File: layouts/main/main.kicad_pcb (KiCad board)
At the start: 4 copper layers, 20.5 x 20.5 mm, 60 parts

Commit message: wip
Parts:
- moved C8 0.36 mm to (3.47, -6.60), turned to 0 degrees
- moved C7 0.22 mm to (3.47, -7.40)
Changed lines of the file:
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@@
 	(footprint "Murata_Electronics_GRM033R60J104KE19D:C0201"
 		(layer "F.Cu")
-		(at 3.67 -6.3 180)
+		(at 3.47 -6.6)
 		(property "Reference" "C8"
 			(at 0 -0.000166 0)
@@
 		(attr through_hole)
 		(fp_line
+			(start -0.69 0.24)
+			(end -0.69 -0.24)
+			(stroke
+				(width 0.15)
+				(type solid)
+			)
+			(layer "F.SilkS")
+		)
+		(fp_line
+			(start -0.53 -0.39)
+			(end -0.17 -0.39)
+			(stroke
+				(width 0.15)
+				(type solid)
+			)
+			(layer "F.SilkS")
+		)
+		(fp_line
+			(start -0.17 0.39)
+			(end -0.53 0.39)
+			(stroke
+				(width 0.15)
+				(type solid)
+			)
+			(layer "F.SilkS")
+		)
+		(fp_line
+			(start 0.17 0.39)
+			(end 0.53 0.39)
+			(stroke
+				(width 0.15)
+				(type solid)
+			)
+			(layer "F.SilkS")
+		)
+		(fp_line
+			(start 0.53 -0.39)
+			(end 0.17 -0.39)
+			(stroke
+				(width 0.15)
+				(type solid)
+			)
+			(layer "F.SilkS")
+		)
+		(fp_line
 			(start 0.69 0.24)
 			(end 0.69 -0.24)
@@
 			(layer "F.SilkS")
 		)
-		(fp_line
+		(fp_arc
+			(start -0.690333 -0.239643)
+			(mid -0.642835 -0.349658)
+			(end -0.53 -0.39)
+			(stroke
+				(width 0.15)
+				(type solid)
+			)
+			(layer "F.SilkS")
+		)
+		(fp_arc
+			(start -0.529667 0.389644)
+			(mid -0.642347 0.349658)
+			(end -0.69 0.24)
+			(stroke
+				(width 0.15)
+				(type solid)
+			)
+			(layer "F.SilkS")
+		)
+		(fp_arc
 			(start 0.53 -0.39)
-			(end 0.17 -0.39)
-			(stroke
-				(width 0.15)
-				(type solid)
-			)
-			(layer "F.SilkS")
-		)
-		(fp_line
-			(start 0.17 0.39)
-			(end 0.53 0.39)
-			(stroke
-				(width 0.15)
-				(type solid)
-			)
-			(layer "F.SilkS")
-		)
-		(fp_line
-			(start -0.17 0.39)
-			(end -0.53 0.39)
-			(stroke
-				(width 0.15)
-				(type solid)
-			)
-			(layer "F.SilkS")
-		)
-		(fp_line
-			(start -0.53 -0.39)
-			(end -0.17 -0.39)
-			(stroke
-				(width 0.15)
-				(type solid)
-			)
-			(layer "F.SilkS")
-		)
-		(fp_line
-			(start -0.69 0.24)
-			(end -0.69 -0.24)
+			(mid 0.642835 -0.349658)
+			(end 0.690333 -0.239643)
 			(stroke
 				(width 0.15)
@@
 			(layer "F.SilkS")
 		)
-		(fp_arc
-			(start 0.53 -0.39)
-			(mid 0.642835 -0.349658)
-			(end 0.690333 -0.239643)
-			(stroke
-				(width 0.15)
-				(type solid)
-			)
-			(layer "F.SilkS")
-		)
-		(fp_arc
-			(start -0.529667 0.389644)
-			(mid -0.642347 0.349658)
-			(end -0.69 0.24)
-			(stroke
-				(width 0.15)
-				(type solid)
-			)
-			(layer "F.SilkS")
-		)
-		(fp_arc
-			(start -0.690333 -0.239643)
-			(mid -0.642835 -0.349658)
-			(end -0.53 -0.39)
-			(stroke
-				(width 0.15)
-				(type solid)
-			)
-			(layer "F.SilkS")
-		)
 		(fp_circle
 			(center -0.3 0.15)
@@
 		)
 		(pad "1" smd rect
-			(at -0.27 0 180)
+			(at -0.27 0)
 			(size 0.37 0.32)
 			(layers "F.Cu" "F.Mask" "F.Paste")
@@
 		)
 		(pad "2" smd rect
-			(at 0.27 0 180)
+			(at 0.27 0)
 			(size 0.37 0.32)
 			(layers "F.Cu" "F.Mask" "F.Paste")
@@
 	(footprint "Murata_Electronics_GRM033R60J104KE19D:C0201"
 		(layer "F.Cu")
-		(at 3.67 -7.3)
+		(at 3.47 -7.4)
 		(property "Reference" "C7"
 			(at 0 -0.000167 0)

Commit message: wip
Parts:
- moved R4 6.52 mm to (-5.80, -4.56), turned to 90 degrees
- moved R2 2.79 mm to (-2.50, -5.86), turned to -90 degrees
- moved REF** 2.39 mm to (-3.80, -6.30)
- moved REF** 1.43 mm to (-6.40, -6.30)
- moved REF** 1.20 mm to (-7.30, -5.30)
- moved R3 0.30 mm to (-2.50, -6.96)
- moved REF** 0.22 mm to (-5.10, -6.30)
- moved R8 0.20 mm to (-3.40, -4.56)
- moved R9 0.20 mm to (-4.60, -4.56)
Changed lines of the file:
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@@
 	(footprint "POGO_PAD:POGO_PAD"
 		(layer "F.Cu")
-		(at -7 -5)
+		(at -6.4 -6.3)
 		(property "Reference" "REF**"
 			(at 0 0 0)
@@
 	(footprint "UNI_ROYAL_0201WMF1002TEE:R0201"
 		(layer "F.Cu")
-		(at -3.2 -4.56 90)
+		(at -3.4 -4.56 90)
 		(property "Reference" "R8"
 			(at 0 0 0)
@@
 	(footprint "POGO_PAD:POGO_PAD"
 		(layer "F.Cu")
-		(at -5.2 -6.1)
+		(at -5.1 -6.3)
 		(property "Reference" "REF**"
 			(at 0 0 0)
@@
 	(footprint "UNI_ROYAL_0201WMF4701TEE:R0201"
 		(layer "F.Cu")
-		(at -2.5 -6.66 -90)
+		(at -2.5 -6.96 -90)
 		(property "Reference" "R3"
 			(at 0 0 0)
@@
 	(footprint "UNI_ROYAL_0201WMJ0330TEE:R0201"
 		(layer "F.Cu")
-		(at 0.66 -3.7)
+		(at -5.8 -4.56 90)
 		(property "Reference" "R4"
-			(at 0 0 90)
+			(at 0 0 0)
 			(layer "F.SilkS")
 			(effects
@@
 		)
 		(property "Value" "33Ω ±5% 50mW"
-			(at 0 0 90)
+			(at 0 0 0)
 			(layer "F.Fab")
 			(effects
@@
 		)
 		(property "Datasheet" "https://wmsc.lcsc.com/wmsc/upload/file/pdf/v2/lcsc/2205312145_UNI-ROYAL-Uniroyal-Elec-0201WMJ0330TEE_C423356.pdf"
-			(at 0 0 0)
+			(at 0 0 90)
 			(layer "User.9")
 			(hide yes)
@@
 		)
 		(property "Description" ""
-			(at 0 0 0)
+			(at 0 0 90)
 			(layer "F.Fab")
 			(hide yes)
@@
 		)
 		(property "checksum" "ab7e766c14a60369aa28116b01504e6514a3eb1616d1f71d480e335b1894b8ea"
-			(at 0 0 90)
+			(at 0 0 0)
 			(layer "User.9")
 			(hide yes)
@@
 		)
 		(property "__atopile_lib_fp_hash__" "5c987cfc-286b-6ffe-d212-f95475017c44"
-			(at 0 0 90)
+			(at 0 0 0)
 			(layer "User.9")
 			(hide yes)
@@
 		)
 		(property "LCSC" "C423356"
-			(at 0 0 0)
+			(at 0 0 90)
 			(layer "User.9")
 			(hide yes)
@@
 		)
 		(property "Manufacturer" "UNI-ROYAL(Uniroyal Elec)"
-			(at 0 0 0)
+			(at 0 0 90)
 			(layer "User.9")
 			(hide yes)
@@
 		)
 		(property "Partnumber" "0201WMJ0330TEE"
-			(at 0 0 0)
+			(at 0 0 90)
 			(layer "User.9")
 			(hide yes)
@@
 		)
 		(property "PARAM_max_power" "{\"type\": \"Quantity_Set_Discrete\", \"data\": {\"intervals\": {\"type\": \"Numeric_Interval_Disjoint\", \"data\": {\"intervals\": [{\"type\": \"Numeric_Interval\", \"data\": {\"min\": 0.05, \"max\": 0.05}}]}}, \"unit\": \"watt\"}}"
-			(at 0 0 0)
+			(at 0 0 90)
 			(layer "User.9")
 			(hide yes)
@@
 		)
 		(property "PARAM_max_voltage" "{\"type\": \"Quantity_Set_Discrete\", \"data\": {\"intervals\": {\"type\": \"Numeric_Interval_Disjoint\", \"data\": {\"intervals\": [{\"type\": \"Numeric_Interval\", \"data\": {\"min\": 25.0, \"max\": 25.0}}]}}, \"unit\": \"volt\"}}"
-			(at 0 0 0)
+			(at 0 0 90)
 			(layer "User.9")
 			(hide yes)
@@
 		)
 		(property "PARAM_resistance" "{\"type\": \"Quantity_Interval_Disjoint\", \"data\": {\"intervals\": {\"type\": \"Numeric_Interval_Disjoint\", \"data\": {\"intervals\": [{\"type\": \"Numeric_Interval\", \"data\": {\"min\": 31.349999975413084, \"max\": 34.650000024586916}}]}}, \"unit\": \"ohm\"}}"
-			(at 0 0 0)
+			(at 0 0 90)
 			(layer "User.9")
 			(hide yes)
@@
 		)
 		(property "atopile_address" "r_nand_clk"
-			(at 0 0 0)
+			(at 0 0 90)
 			(layer "User.9")
 			(hide yes)
@@
 		(attr through_hole)
 		(fp_line
-			(start -0.62 -0.39)
-			(end -0.17 -0.39)
+			(start 0.62 -0.39)
+			(end 0.17 -0.39)
 			(stroke
 				(width 0.15)
@@
 		)
 		(fp_line
-			(start -0.62 0.39)
-			(end -0.62 -0.39)
+			(start -0.62 -0.39)
+			(end -0.17 -0.39)
 			(stroke
 				(width 0.15)
@@
 		)
 		(fp_line
-			(start -0.17 0.39)
-			(end -0.62 0.39)
+			(start 0.62 0.39)
+			(end 0.62 -0.39)
 			(stroke
 				(width 0.15)
@@
 		)
 		(fp_line
-			(start 0.62 -0.39)
-			(end 0.17 -0.39)
+			(start -0.17 0.39)
+			(end -0.62 0.39)
 			(stroke
 				(width 0.15)
@@
 		)
 		(fp_line
-			(start 0.62 0.39)
-			(end 0.62 -0.39)
+			(start -0.62 0.39)
+			(end -0.62 -0.39)
 			(stroke
 				(width 0.15)
@@
 		)
 		(fp_text user "${REFERENCE}"
-			(at 0 0 90)
+			(at 0 0 0)
 			(layer "F.SilkS")
 			(effects
@@
 		)
 		(fp_text user "${REFERENCE}"
-			(at 0 0 90)
+			(at 0 0 0)
 			(layer "F.Fab")
 			(effects
@@
 		)
 		(pad "1" smd rect
-			(at -0.24 0)
+			(at -0.24 0 90)
 			(size 0.3 0.32)
 			(layers "F.Cu" "F.Mask" "F.Paste")
@@
 		)
 		(pad "2" smd rect
-			(at 0.24 0)
+			(at 0.24 0 90)
 			(size 0.3 0.32)
 			(layers "F.Cu" "F.Mask" "F.Paste")
@@
 	(footprint "POGO_PAD:POGO_PAD"
 		(layer "F.Cu")
-		(at -6.4 -6.1)
+		(at -7.3 -5.3)
 		(property "Reference" "REF**"
 			(at 0 0 0)
@@
 	(footprint "POGO_PAD:POGO_PAD"
 		(layer "F.Cu")
-		(at -5.8 -5)
+		(at -3.8 -6.3)
 		(property "Reference" "REF**"
 			(at 0 0 0)
@@
 	(footprint "UNI_ROYAL_0201WMF4701TEE:R0201"
 		(layer "F.Cu")
-		(at -0.74 -3.7)
+		(at -2.5 -5.86 -90)
 		(property "Reference" "R2"
-			(at 0 0 0)
+			(at 0 0 90)
 			(layer "F.SilkS")
 			(effects
@@
 		)
 		(property "Value" "4.7kΩ ±1% 50mW"
-			(at 0 0 0)
+			(at 0 0 90)
 			(layer "F.Fab")
 			(effects
@@
 		)
 		(property "Datasheet" "https://wmsc.lcsc.com/wmsc/upload/file/pdf/v2/lcsc/2205311945_UNI-ROYAL-Uniroyal-Elec-0201WMF4701TEE_C270346.pdf"
-			(at 0 0 0)
+			(at 0 0 90)
 			(layer "User.9")
 			(hide yes)
@@
 		)
 		(property "Description" ""
-			(at 0 0 0)
+			(at 0 0 90)
 			(layer "F.Fab")
 			(hide yes)
@@
 		)
 		(property "checksum" "8334129e8d68cc94feb6f24d4494287d4e5c79980c878904c53191d3ecd9f05e"
-			(at 0 0 0)
+			(at 0 0 90)
 			(layer "User.9")
 			(hide yes)
@@
 		)
 		(property "__atopile_lib_fp_hash__" "2b7c5f96-36d0-b881-fd7f-66c187796e91"
-			(at 0 0 0)
+			(at 0 0 90)
 			(layer "User.9")
 			(hide yes)
@@
 		)
 		(property "LCSC" "C270346"
-			(at 0 0 0)
+			(at 0 0 90)
 			(layer "User.9")
 			(hide yes)
@@
 		)
 		(property "Manufacturer" "UNI-ROYAL(Uniroyal Elec)"
-			(at 0 0 0)
+			(at 0 0 90)
 			(layer "User.9")
 			(hide yes)
@@
 		)
 		(property "Partnumber" "0201WMF4701TEE"
-			(at 0 0 0)
+			(at 0 0 90)
 			(layer "User.9")
 			(hide yes)
@@
 		)
 		(property "PARAM_max_power" "{\"type\": \"Quantity_Set_Discrete\", \"data\": {\"intervals\": {\"type\": \"Numeric_Interval_Disjoint\", \"data\": {\"intervals\": [{\"type\": \"Numeric_Interval\", \"data\": {\"min\": 0.05, \"max\": 0.05}}]}}, \"unit\": \"watt\"}}"
-			(at 0 0 0)
+			(at 0 0 90)
 			(layer "User.9")
 			(hide yes)
@@
 		)
 		(property "PARAM_max_voltage" "{\"type\": \"Quantity_Set_Discrete\", \"data\": {\"intervals\": {\"type\": \"Numeric_Interval_Disjoint\", \"data\": {\"intervals\": [{\"type\": \"Numeric_Interval\", \"data\": {\"min\": 25.0, \"max\": 25.0}}]}}, \"unit\": \"volt\"}}"
-			(at 0 0 0)
+			(at 0 0 90)
 			(layer "User.9")
 			(hide yes)
@@
 		)
 		(property "PARAM_resistance" "{\"type\": \"Quantity_Interval_Disjoint\", \"data\": {\"intervals\": {\"type\": \"Numeric_Interval_Disjoint\", \"data\": {\"intervals\": [{\"type\": \"Numeric_Interval\", \"data\": {\"min\": 4653.000001050532, \"max\": 4746.999998949468}}]}}, \"unit\": \"ohm\"}}"
-			(at 0 0 0)
+			(at 0 0 90)
 			(layer "User.9")
 			(hide yes)
@@
 		)
 		(property "atopile_address" "r_i2c_scl"
-			(at 0 0 0)
+			(at 0 0 90)
 			(layer "User.9")
 			(hide yes)
@@
 		(attr through_hole)
 		(fp_line
-			(start -0.62 -0.39)
-			(end -0.17 -0.39)
+			(start -0.62 0.39)
+			(end -0.62 -0.39)
 			(stroke
 				(width 0.15)
@@
 		)
 		(fp_line
-			(start -0.62 0.39)
-			(end -0.62 -0.39)
+			(start -0.17 0.39)
+			(end -0.62 0.39)
 			(stroke
 				(width 0.15)
@@
 		)
 		(fp_line
-			(start -0.17 0.39)
-			(end -0.62 0.39)
+			(start 0.17 0.39)
+			(end 0.62 0.39)
 			(stroke
 				(width 0.15)
@@
 		)
 		(fp_line
-			(start 0.17 0.39)
-			(end 0.62 0.39)
+			(start 0.62 0.39)
+			(end 0.62 -0.39)
 			(stroke
 				(width 0.15)
@@
 		)
 		(fp_line
-			(start 0.62 -0.39)
-			(end 0.17 -0.39)
+			(start -0.62 -0.39)
+			(end -0.17 -0.39)
 			(stroke
 				(width 0.15)
@@
 		)
 		(fp_line
-			(start 0.62 0.39)
-			(end 0.62 -0.39)
+			(start 0.62 -0.39)
+			(end 0.17 -0.39)
 			(stroke
 				(width 0.15)
@@
 		)
 		(fp_text user "${REFERENCE}"
-			(at 0 0 0)
+			(at 0 0 90)
 			(layer "F.SilkS")
 			(effects
@@
 		)
 		(fp_text user "${REFERENCE}"
-			(at 0 0 0)
+			(at 0 0 90)
 			(layer "F.Fab")
 			(effects
@@
 		)
 		(pad "1" smd rect
-			(at -0.24 0)
+			(at -0.24 0 270)
 			(size 0.3 0.32)
 			(layers "F.Cu" "F.Mask" "F.Paste")
@@
 		)
 		(pad "2" smd rect
-			(at 0.24 0)
+			(at 0.24 0 270)
 			(size 0.3 0.32)
 			(layers "F.Cu" "F.Mask" "F.Paste")
@@
 	(footprint "UNI_ROYAL_0201WMF1002TEE:R0201"
 		(layer "F.Cu")
-		(at -4.4 -4.56 90)
+		(at -4.6 -4.56 90)
 		(property "Reference" "R9"
 			(at 0 0 0)

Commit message: wip
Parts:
- moved C13 1.25 mm to (4.80, -3.33)
- moved R14 0.84 mm to (2.40, -3.26)
- moved C21 0.54 mm to (4.10, -3.52), turned to 90 degrees
- moved R10 0.20 mm to (-0.76, -2.50)
- moved R13 0.09 mm to (0.66, -2.50)
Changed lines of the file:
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@@
 	(footprint "UNI_ROYAL_0201WMF0000TEE:R0201"
 		(layer "F.Cu")
-		(at -0.5625 -2.55 180)
+		(at -0.76 -2.5 180)
 		(property "Reference" "R10"
 			(at 0 0 0)
@@
 	(footprint "YAGEO_RC0201FR_07150KL:R0201"
 		(layer "F.Cu")
-		(at 3.2375 -3.21 90)
+		(at 2.4 -3.26 90)
 		(property "Reference" "R14"
 			(at 0 0 0)
@@
 	(footprint "Murata_Electronics_GRM033R60J104KE19D:C0201"
 		(layer "F.Cu")
-		(at 6.0375 -3.48 90)
+		(at 4.8 -3.33 90)
 		(property "Reference" "C13"
 			(at 0 -0.000166 90)
@@
 	(footprint "Samsung_Electro_Mechanics_CL05A105KA5NQNC:C0402"
 		(layer "F.Cu")
-		(at 4.6175 -3.35 180)
+		(at 4.1 -3.52 90)
 		(property "Reference" "C21"
-			(at 0 0 0)
+			(at 0 0 90)
 			(layer "F.SilkS")
 			(effects
@@
 		)
 		(property "Value" "1µF ±10% 25V X5R"
-			(at 0 0 0)
+			(at 0 0 90)
 			(layer "F.Fab")
 			(effects
@@
 		)
 		(property "Datasheet" "https://www.lcsc.com/datasheet/lcsc_datasheet_2304140030_Samsung-Electro-Mechanics-CL05A105KA5NQNC_C52923.pdf"
-			(at 0 0 0)
+			(at 0 0 90)
 			(layer "User.9")
 			(hide yes)
@@
 		)
 		(property "Description" ""
-			(at 0 0 0)
+			(at 0 0 90)
 			(layer "F.Fab")
 			(hide yes)
@@
 		)
 		(property "checksum" "c4552cab8ba94b7b2294d619195d3584771a66b6df67e026bc6e8196d517b938"
-			(at 0 0 0)
+			(at 0 0 90)
 			(layer "User.9")
 			(hide yes)
@@
 		)
 		(property "__atopile_lib_fp_hash__" "e1042a3b-4b38-6816-2d7d-270ba4226139"
-			(at 0 0 0)
+			(at 0 0 90)
 			(layer "User.9")
 			(hide yes)
@@
 		)
 		(property "LCSC" "C52923"
-			(at 0 0 0)
+			(at 0 0 90)
 			(layer "User.9")
 			(hide yes)
@@
 		)
 		(property "Manufacturer" "Samsung Electro-Mechanics"
-			(at 0 0 0)
+			(at 0 0 90)
 			(layer "User.9")
 			(hide yes)
@@
 		)
 		(property "Partnumber" "CL05A105KA5NQNC"
-			(at 0 0 0)
+			(at 0 0 90)
 			(layer "User.9")
 			(hide yes)
@@
 		)
 		(property "PARAM_capacitance" "{\"type\": \"Quantity_Interval_Disjoint\", \"data\": {\"intervals\": {\"type\": \"Numeric_Interval_Disjoint\", \"data\": {\"intervals\": [{\"type\": \"Numeric_Interval\", \"data\": {\"min\": 8.99999999e-07, \"max\": 1.100000001e-06}}]}}, \"unit\": \"farad\"}}"
-			(at 0 0 0)
+			(at 0 0 90)
 			(layer "User.9")
 			(hide yes)
@@
 		)
 		(property "PARAM_max_voltage" "{\"type\": \"Quantity_Set_Discrete\", \"data\": {\"intervals\": {\"type\": \"Numeric_Interval_Disjoint\", \"data\": {\"intervals\": [{\"type\": \"Numeric_Interval\", \"data\": {\"min\": 25.0, \"max\": 25.0}}]}}, \"unit\": \"volt\"}}"
-			(at 0 0 0)
+			(at 0 0 90)
 			(layer "User.9")
 			(hide yes)
@@
 		)
 		(property "PARAM_temperature_coefficient" "{\"type\": \"EnumSet\", \"data\": {\"elements\": [{\"name\": \"X5R\"}], \"enum\": {\"name\": \"TemperatureCoefficient\", \"values\": {\"Y5V\": 1, \"Z5U\": 2, \"X7S\": 3, \"X5R\": 4, \"X6R\": 5, \"X7R\": 6, \"X8R\": 7, \"C0G\": 8}}}}"
-			(at 0 0 0)
+			(at 0 0 90)
 			(layer "User.9")
 			(hide yes)
@@
 		)
 		(property "atopile_address" "c_vddio_bulk"
-			(at 0 0 0)
+			(at 0 0 90)
 			(layer "User.9")
 			(hide yes)
@@
 		(attr smd)
 		(fp_line
-			(start 0.87 -0.35)
-			(end 0.87 0.35)
+			(start 0.22 -0.5)
+			(end 0.72 -0.5)
 			(stroke
 				(width 0.15)
@@
 		)
 		(fp_line
-			(start 0.72 0.5)
-			(end 0.22 0.5)
+			(start -0.72 -0.5)
+			(end -0.22 -0.5)
 			(stroke
 				(width 0.15)
@@
 		)
 		(fp_line
-			(start 0.22 -0.5)
-			(end 0.72 -0.5)
+			(start 0.87 -0.35)
+			(end 0.87 0.35)
 			(stroke
 				(width 0.15)
@@
 		)
 		(fp_line
-			(start -0.22 0.5)
-			(end -0.72 0.5)
+			(start -0.87 0.35)
+			(end -0.87 -0.35)
 			(stroke
 				(width 0.15)
@@
 		)
 		(fp_line
-			(start -0.72 -0.5)
-			(end -0.22 -0.5)
+			(start 0.72 0.5)
+			(end 0.22 0.5)
 			(stroke
 				(width 0.15)
@@
 		)
 		(fp_line
-			(start -0.87 0.35)
-			(end -0.87 -0.35)
+			(start -0.22 0.5)
+			(end -0.72 0.5)
 			(stroke
 				(width 0.15)
@@
 		)
 		(fp_arc
-			(start 0.87 0.35)
-			(mid 0.826066 0.456066)
-			(end 0.72 0.5)
+			(start 0.72 -0.5)
+			(mid 0.826066 -0.456066)
+			(end 0.87 -0.35)
 			(stroke
 				(width 0.15)
@@
 		)
 		(fp_arc
-			(start 0.72 -0.5)
-			(mid 0.826066 -0.456066)
-			(end 0.87 -0.35)
+			(start -0.87 -0.35)
+			(mid -0.826066 -0.456066)
+			(end -0.72 -0.5)
 			(stroke
 				(width 0.15)
@@
 		)
 		(fp_arc
-			(start -0.72 0.5)
-			(mid -0.826066 0.456066)
-			(end -0.87 0.35)
+			(start 0.87 0.35)
+			(mid 0.826066 0.456066)
+			(end 0.72 0.5)
 			(stroke
 				(width 0.15)
@@
 		)
 		(fp_arc
-			(start -0.87 -0.35)
-			(mid -0.826066 -0.456066)
-			(end -0.72 -0.5)
+			(start -0.72 0.5)
+			(mid -0.826066 0.456066)
+			(end -0.87 0.35)
 			(stroke
 				(width 0.15)
@@
 		)
 		(fp_text user "${REFERENCE}"
-			(at 0 0 0)
+			(at 0 0 90)
 			(layer "F.SilkS")
 			(effects
@@
 		)
 		(fp_text user "${REFERENCE}"
-			(at 0 0 0)
+			(at 0 0 90)
 			(layer "F.Fab")
 			(effects
@@
 		)
 		(pad "1" smd rect
-			(at -0.42 0 180)
+			(at -0.42 0 90)
 			(size 0.5 0.54)
 			(layers "F.Cu" "F.Mask" "F.Paste")
@@
 		)
 		(pad "2" smd rect
-			(at 0.42 0 180)
+			(at 0.42 0 90)
 			(size 0.5 0.54)
 			(layers "F.Cu" "F.Mask" "F.Paste")
@@
 		(at 6.7 -5.5)
 		(property "Reference" "REF**"
-			(at 1.3 0 0)
+			(at 0 0 0)
 			(layer "F.SilkS")
 			(effects
@@
 	(footprint "UNI_ROYAL_0201WMF4702TEE:R0201"
 		(layer "F.Cu")
-		(at 0.7375 -2.55 180)
+		(at 0.66 -2.5 180)
 		(property "Reference" "R13"
 			(at 0 0 90)

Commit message: wip
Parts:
- moved C11 0.28 mm to (-2.38, 5.00)
- moved C10 0.10 mm to (-3.60, 5.17)
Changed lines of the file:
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@@
 	(footprint "Murata_Electronics_GRM033R60J104KE19D:C0201"
 		(layer "F.Cu")
-		(at -3.6 5.27 -90)
+		(at -3.6 5.17 -90)
 		(property "Reference" "C10"
 			(at 0 -0.000167 0)
@@
 	(footprint "Samsung_Electro_Mechanics_CL05A225MQ5NSNC:C0402"
 		(layer "F.Cu")
-		(at -2.18 5.2)
+		(at -2.38 5)
 		(property "Reference" "C11"
 			(at 0 0 90)

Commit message: wip
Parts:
- moved R15 0.36 mm to (-1.20, 6.52)
- moved R11 0.20 mm to (-3.56, 8.80)
- moved C6 0.11 mm to (-5.63, 6.80)
- moved C5 0.10 mm to (-1.50, 7.97)
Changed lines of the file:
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@@
 	(footprint "Murata_Electronics_GRM033R60J104KE19D:C0201"
 		(layer "F.Cu")
-		(at -5.67 6.7 180)
+		(at -5.63 6.8 180)
 		(property "Reference" "C6"
 			(at 0 -0.000166 0)
@@
 	(footprint "UNI_ROYAL_0201WMJ0330TEE:R0201"
 		(layer "F.Cu")
-		(at -3.76 8.8)
+		(at -3.56 8.8)
 		(property "Reference" "R11"
 			(at 0 0 90)
@@
 	(footprint "DNP_RES_0201:DNP_RES_0201"
 		(layer "F.Cu")
-		(at -1.4 6.82 -90)
+		(at -1.2 6.52 -90)
 		(property "Reference" "R15"
 			(at 0 0 90)
@@
 	(footprint "Murata_Electronics_GRM033R60J104KE19D:C0201"
 		(layer "F.Cu")
-		(at -1.4 7.97 -90)
+		(at -1.5 7.97 -90)
 		(property "Reference" "C5"
 			(at 0 -0.000167 90)

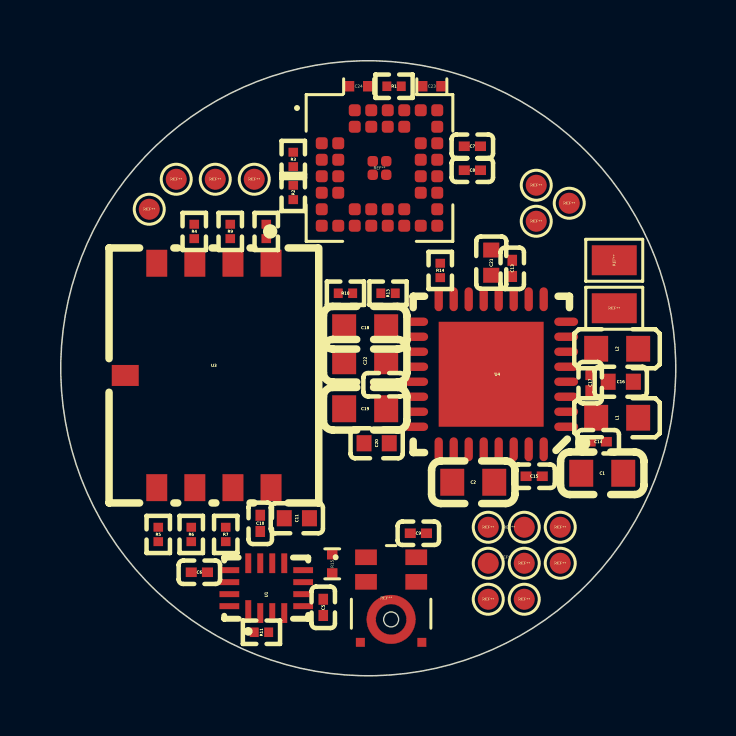
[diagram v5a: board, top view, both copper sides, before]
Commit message: assign reference designators to mcu and mic
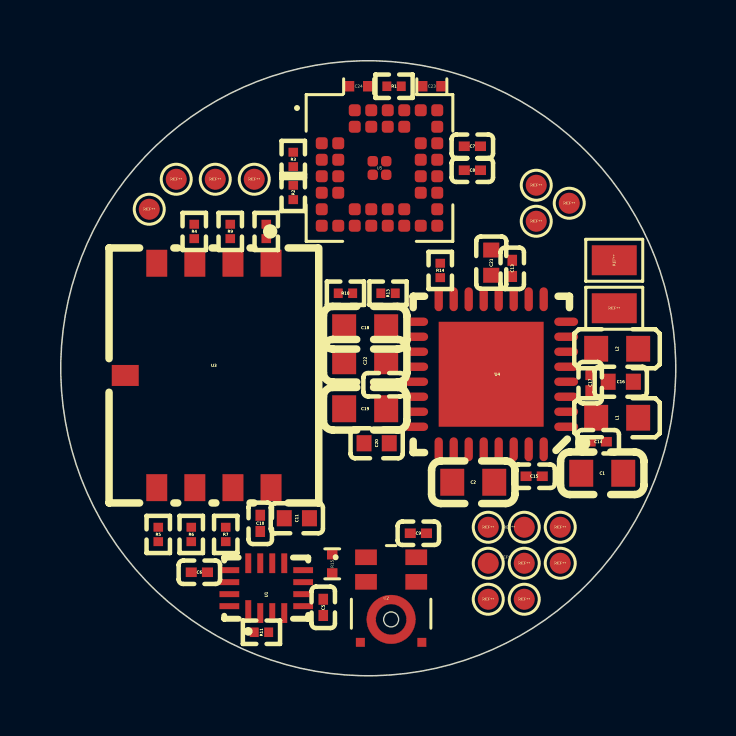
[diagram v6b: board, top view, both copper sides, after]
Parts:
- renumbered REF** to U2, REF** to U5
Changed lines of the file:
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@@
 		(layer "F.Cu")
 		(at 0.7625 7.662)
-		(property "Reference" "REF**"
+		(property "Reference" "U2"
 			(at -0.1625 0 0)
 			(layer "F.SilkS")
@@
 		(layer "F.Cu")
 		(at 0.375 -6.675)
-		(property "Reference" "REF**"
-			(at 0 0 0)
-			(layer "F.SilkS")
+		(property "Reference" "U5"
+			(at 0 0 0)
+			(layer "F.SilkS")
